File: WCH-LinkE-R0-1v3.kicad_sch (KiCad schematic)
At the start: 38 parts, among them Q1 DMG1012UW-7, Q2 DMG1012UW-7, SW1 12V 50mA, SW2 12V 50mA, SW3 12V 50mA, U3 CH32V305FBP6

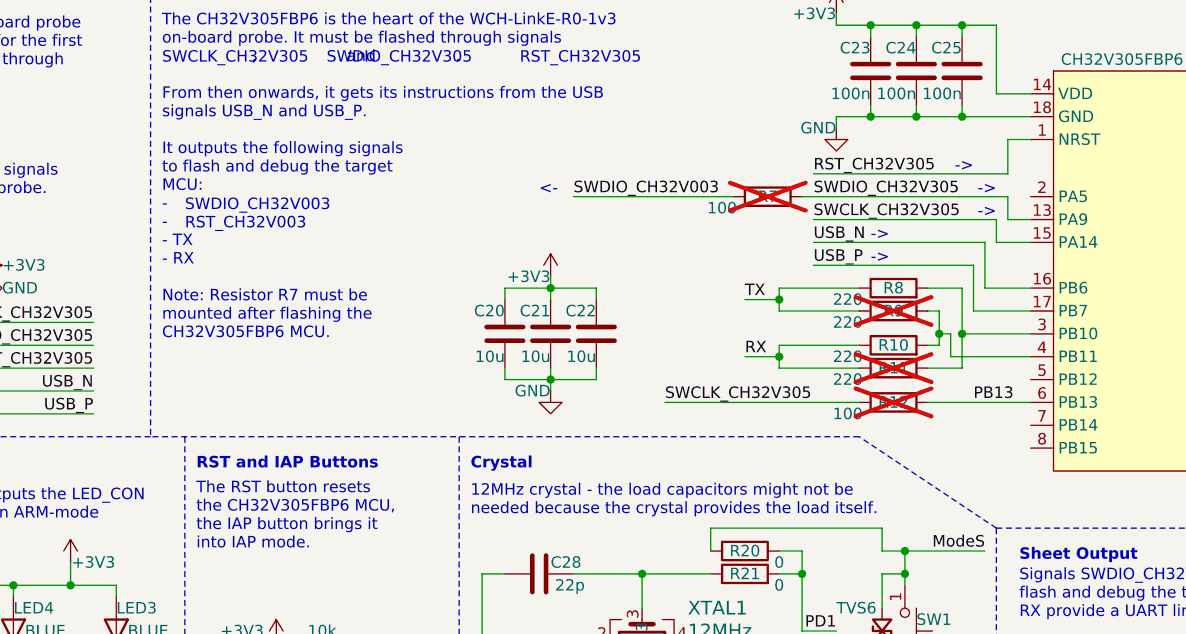
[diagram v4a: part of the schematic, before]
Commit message: Work on BOM
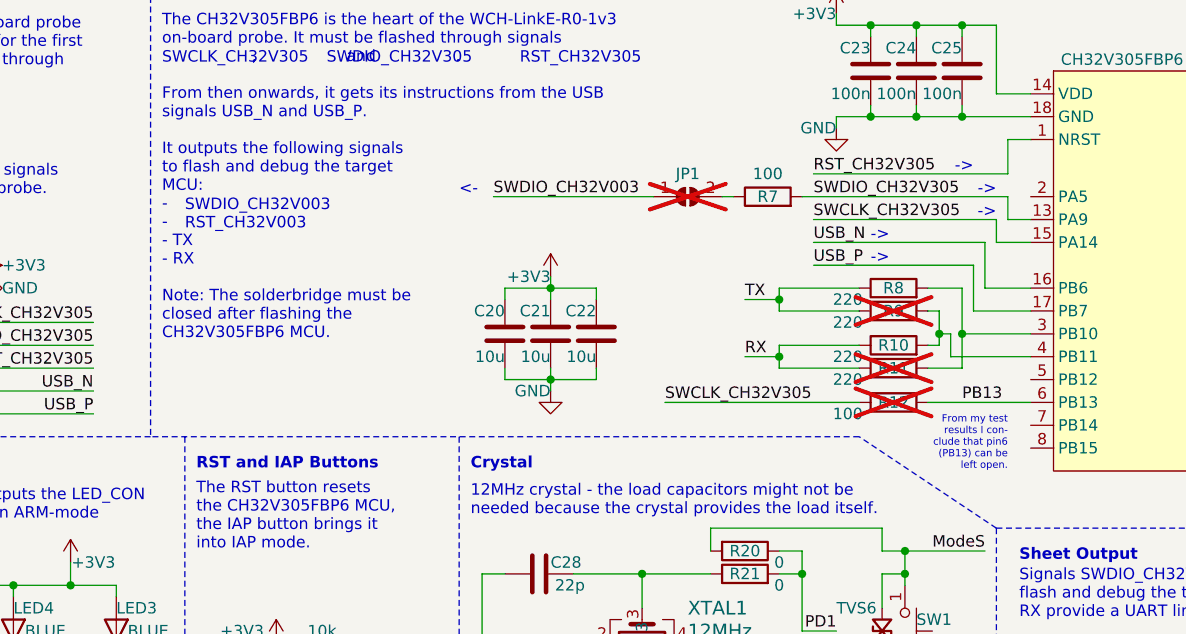
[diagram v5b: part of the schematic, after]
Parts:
- added JP1: SolderJumper_2_Open, Tiny_Scarab:SOLDER_BRIDGE, symbol Jumper:SolderJumper_2_Open
- LED3, LED4: JLCPCB Part # (none) -> C6538602
- R7: now fitted; now in the parts list
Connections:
- net SWDIO_CH32V003: now also JP1.1 (A); no longer R7.1
- new net: JP1.2 (B), R7.1
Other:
- note added: "From my test results I con- clude that pin6 (PB13) can be left open."
- note added: "The CH32V305FBP6 is the heart of the WCH-LinkE-R0-1v3 on-board probe. It must be flashed through signals , and . From then onwards, it gets its instructions from the USB signals USB_N and USB_P. It outputs the following signals to flash and debug the target MCU: - - - TX - RX Note: The solderbridge must be closed after flashing the CH32V305FBP6 MCU."
- note removed: "The CH32V305FBP6 is the heart of the WCH-LinkE-R0-1v3 on-board probe. It must be flashed through signals , and . From then onwards, it gets its instructions from the USB signals USB_N and USB_P. It outputs the following signals to flash and debug the target MCU: - - - TX - RX Note: Resistor R7 must be mounted after flashing the CH32V305FBP6 MCU."
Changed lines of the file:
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@@
-    (stroke (width 0) (type default))
-  )
-  (wire (pts (xy 142.24 67.31) (xy 153.67 67.31))
     (stroke (width 0) (type default))
   )
@@
     (stroke (width 0) (type default))
   )
+  (wire (pts (xy 142.24 67.31) (xy 153.67 67.31))
+    (stroke (width 0) (type default))
+  )
   (wire (pts (xy 49.53 68.58) (xy 31.75 68.58))
     (stroke (width 0) (type default))
@@
     (stroke (width 0) (type default))
   )
+  (wire (pts (xy 93.98 44.45) (xy 111.76 44.45))
+    (stroke (width 0) (type default))
+  )
   (wire (pts (xy 77.47 124.46) (xy 77.47 121.92))
     (stroke (width 0) (type default))
@@
     (stroke (width 0) (type default))
   )
+  (wire (pts (xy 119.38 44.45) (xy 120.65 44.45))
+    (stroke (width 0) (type default))
+  )
   (wire (pts (xy 128.27 83.82) (xy 128.27 86.36))
     (stroke (width 0) (type default))
@@
   )
   (wire (pts (xy 100.33 53.34) (xy 100.33 54.61))
-    (stroke (width 0) (type default))
-  )
-  (wire (pts (xy 102.87 44.45) (xy 120.65 44.45))
     (stroke (width 0) (type default))
   )
@@
     (effects (font (size 1.27 1.27) (color 194 0 194 1)) (justify left bottom))
   )
-  (text "<-" (at 99.06 44.45 0)
+  (text "<-" (at 90.17 44.45 0)
     (effects (font (size 1.27 1.27) (color 221 133 0 1)) (justify left bottom))
   )
@@
     (effects (font (size 1.27 1.27) (color 0 0 0 1)) (justify left bottom))
   )
-  (text "The CH32V305FBP6 is the heart of the WCH-LinkE-R0-1v3\non-board probe. It must be flashed through signals\n                  ,                  and                .\n\nFrom then onwards, it gets its instructions from the USB\nsignals USB_N and USB_P.\n\nIt outputs the following signals\nto flash and debug the target\nMCU:\n-\n-\n- TX\n- RX\n\nNote: Resistor R7 must be\nmounted after flashing the\nCH32V305FBP6 MCU."
+  (text "The CH32V305FBP6 is the heart of the WCH-LinkE-R0-1v3\non-board probe. It must be flashed through signals\n                  ,                  and                .\n\nFrom then onwards, it gets its instructions from the USB\nsignals USB_N and USB_P.\n\nIt outputs the following signals\nto flash and debug the target\nMCU:\n-\n-\n- TX\n- RX\n\nNote: The solderbridge must be\nclosed after flashing the\nCH32V305FBP6 MCU."
     (at 57.15 60.452 0)
     (effects (font (size 1.27 1.27)) (justify left bottom))
@@
     (effects (font (size 1.27 1.27)) (justify left bottom))
   )
+  (text "From my test\nresults I con-\nclude that pin6\n(PB13) can be\nleft open."
+    (at 151.13 74.93 0)
+    (effects (font (size 0.8 0.8)) (justify right bottom))
+  )
   (text "SWCLK_CH32V305" (at 16.51 34.29 0)
     (effects (font (size 1.27 1.27) (color 194 0 194 1)) (justify left bottom))
@@
     (effects (font (size 1.27 1.27)) (justify left bottom))
   )
-  (label "PB13" (at 147.32 67.31 0) (fields_autoplaced)
+  (label "PB13" (at 146.05 67.31 0) (fields_autoplaced)
     (effects (font (size 1.27 1.27)) (justify left bottom))
   )
-  (label "SWDIO_CH32V003" (at 102.87 44.45 0) (fields_autoplaced)
+  (label "SWDIO_CH32V003" (at 93.98 44.45 0) (fields_autoplaced)
     (effects (font (size 1.27 1.27) (color 221 133 0 1)) (justify left bottom))
   )
@@
       (effects (font (size 1.27 1.27)) hide)
     )
-    (property "JLCPCB Part #" "" (at 39.37 92.71 0)
+    (property "JLCPCB Part #" "C6538602" (at 39.37 92.71 0)
       (effects (font (size 1.27 1.27)) hide)
     )
@@
     )
   )
+  (symbol (lib_id "Jumper:SolderJumper_2_Open") (at 115.57 44.45 0) (unit 1)
+    (in_bom no) (on_board yes) (dnp yes)
+    (property "Reference" "JP1" (at 115.57 41.91 0)
+      (effects (font (size 1.27 1.27)))
+    )
+    (property "Value" "SolderJumper_2_Open" (at 115.57 40.64 0)
+      (effects (font (size 1.27 1.27)) hide)
+    )
+    (property "Footprint" "Tiny_Scarab:SOLDER_BRIDGE" (at 115.57 44.45 0)
+      (effects (font (size 1.27 1.27)) hide)
+    )
+    (property "Datasheet" "~" (at 115.57 44.45 0)
+      (effects (font (size 1.27 1.27)) hide)
+    )
+    (pin "2")
+    (pin "1")
+    (instances
+      (project "tiny-scarab"
+        (path "/156c5422-ee07-49a4-8263-a2dbd26b90bd/90393844-9805-4207-88e8-abd4029c5b43"
+          (reference "JP1") (unit 1)
+        )
+      )
+    )
+  )
   (symbol (lib_id "Tiny_Scarab:LED_BLUE_CSL0902BT") (at 40.64 92.71 90) (unit 1)
     (in_bom yes) (on_board yes) (dnp no)
@@
       (effects (font (size 1.27 1.27)) hide)
     )
-    (property "JLCPCB Part #" "" (at 27.94 92.71 0)
+    (property "JLCPCB Part #" "C6538602" (at 27.94 92.71 0)
       (effects (font (size 1.27 1.27)) hide)
     )
@@
   )
   (symbol (lib_id "Device:R") (at 124.46 44.45 90) (unit 1)
-    (in_bom no) (on_board yes) (dnp yes)
+    (in_bom yes) (on_board yes) (dnp no)
     (property "Reference" "R7" (at 124.46 44.45 90)
       (effects (font (size 1.27 1.27)))
     )
-    (property "Value" "100" (at 119.38 45.72 90)
-      (effects (font (size 1.27 1.27)))
-    )
+    (property "Value" "100" (at 124.46 41.91 90)
+      (effects (font (size 1.27 1.27)))
+    )

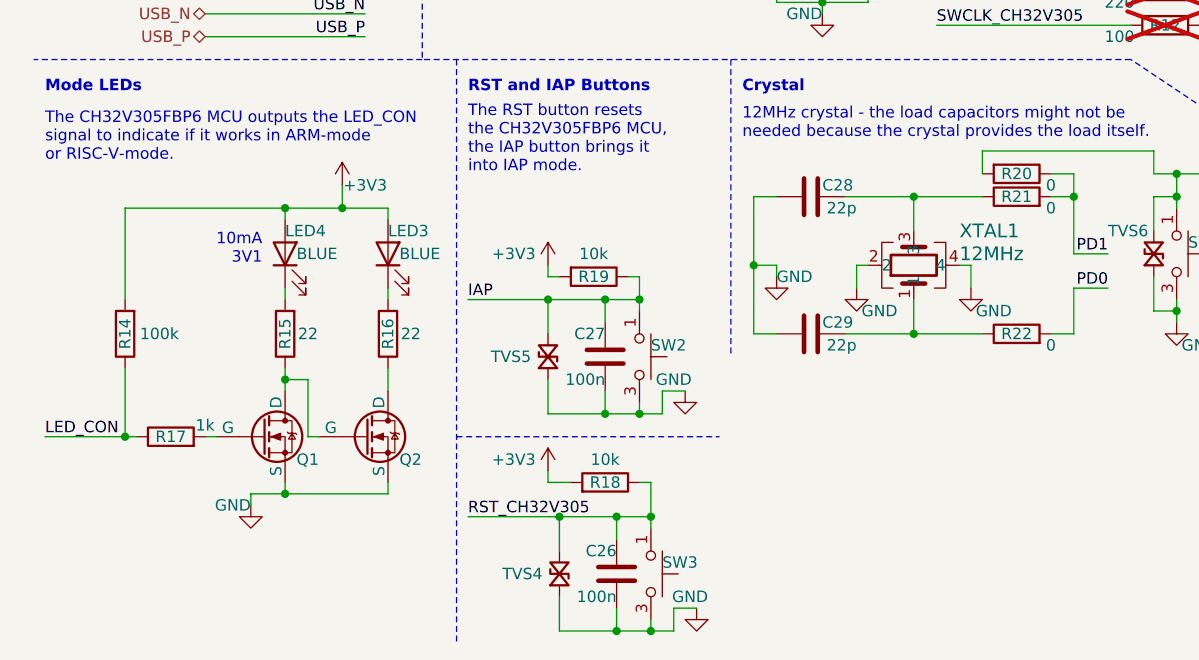
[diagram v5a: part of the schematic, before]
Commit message: Modify resistors for LEDs
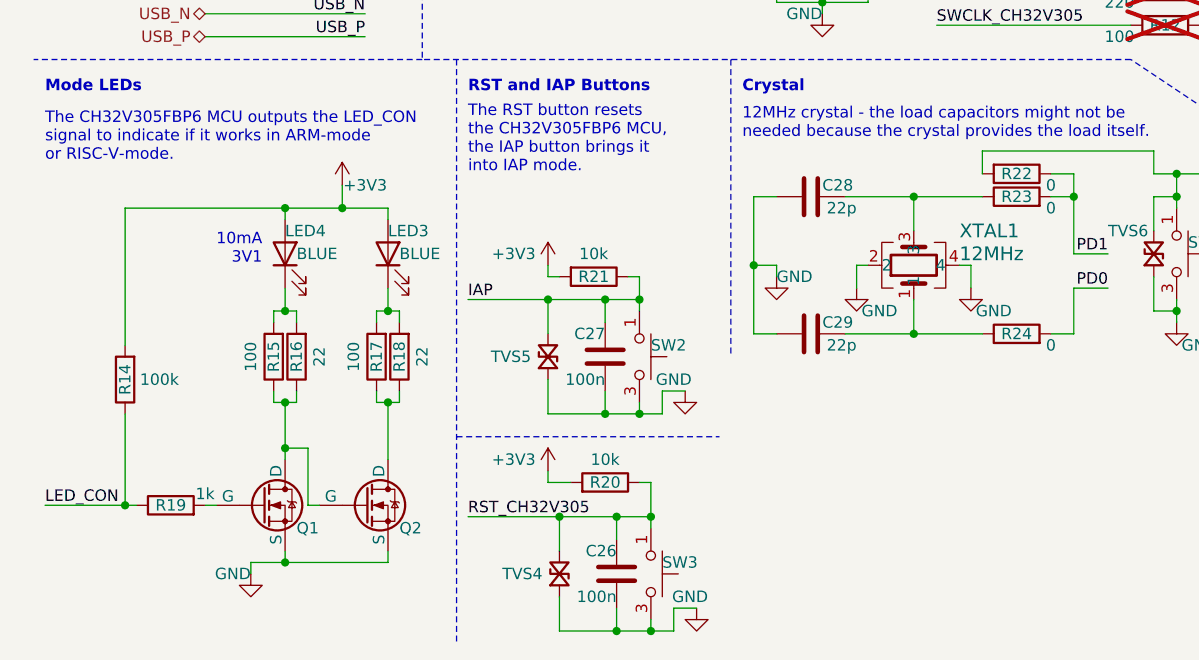
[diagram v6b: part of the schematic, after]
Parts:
- added R15, R17: 100, Resistor_SMD:R_0402_1005Metric_Pad0.72x0.64mm_HandSolder, symbol Device:R
- renumbered R15 to R16, R16 to R18, R17 to R19, R18 to R20, R19 to R21, R20 to R22, R21 to R23, R22 to R24
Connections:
- net at LED3.1 (K), R18.2: now also R17.2
- net at LED4.1 (K), R16.2: now also R15.2
- net at Q1.3 (D), Q2.1 (G), R16.1: now also R15.1
- net at Q2.3 (D), R18.1: now also R17.1
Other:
- moved on the sheet: Q1, Q2, R14, R16, R18, R19

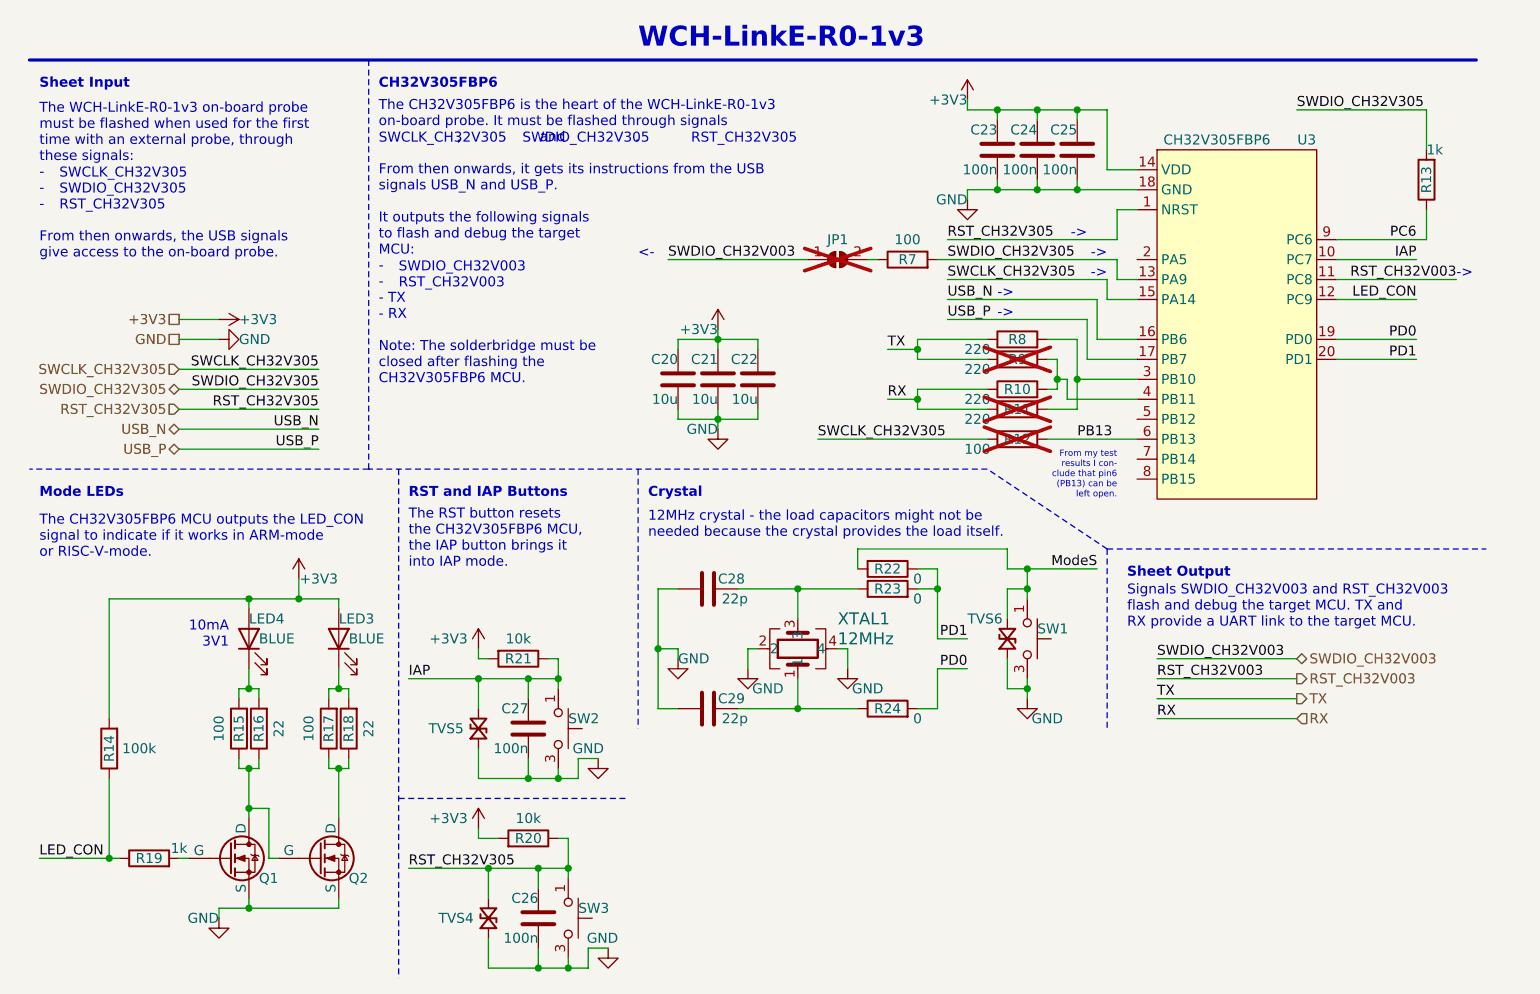
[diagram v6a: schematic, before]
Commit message: Rename 'modify_designators.py' into 'kicad_designators.py'
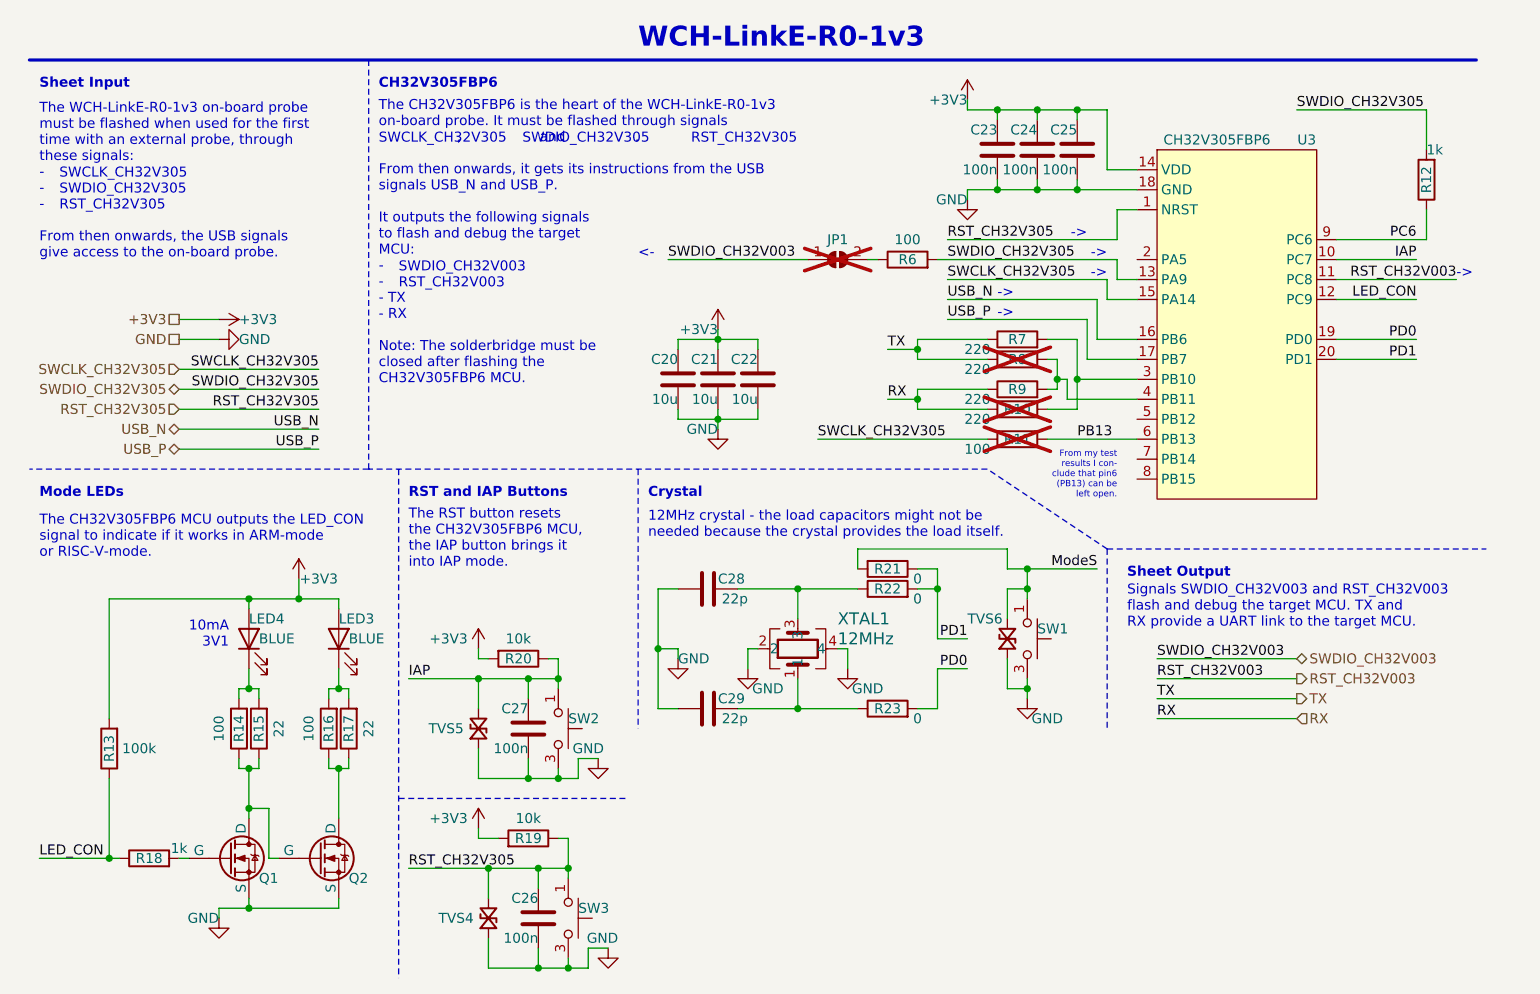
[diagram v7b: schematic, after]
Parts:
- renumbered R11 to R10, R12 to R11, R13 to R12, R14 to R13, R15 to R14, R16 to R15, R17 to R16, R18 to R17, R19 to R18, R20 to R19, R21 to R20, R22 to R21, R23 to R22, R24 to R23, R7 to R6, R8 to R7, R9 to R8, R10 to R9

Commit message: Adapt project to KiCAD 8
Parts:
- U3: footprint Package_SO:TSSOP-20_4.4x6.5mm_P0.65mm -> Tiny_Scarab:TSSOP-20_4.4x6.5mm_P0.65mm
